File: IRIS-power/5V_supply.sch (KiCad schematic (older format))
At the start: 8 parts

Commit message: Finalized power board V2 schematic, preparing to layout
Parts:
- C501, C502: renamed from C?; footprint (none) -> Capacitor_SMD:C_0603_1608Metric
- C503, C504: renamed from C?; footprint (none) -> Capacitor_SMD:C_1210_3225Metric
- NT501: renamed from NT?; footprint (none) -> NetTie:NetTie-2_SMD_Pad0.5mm
- R501, R502: renamed from R?; footprint (none) -> Resistor_SMD:R_0603_1608Metric
- U501: renamed from U?; footprint (none) -> star-common-lib:TPSM53604
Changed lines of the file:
@@
 $Descr A4 11693 8268
 encoding utf-8
-Sheet 4 9
+Sheet 5 8
 Title ""
 Date ""
@@
 P 5700 3950
 AR Path="/5F427B86" Ref="U?"  Part="1"
-AR Path="/5F41B5C3/5F427B86" Ref="U?"  Part="1"
-F 0 "U?" H 5700 4400 50  0000 C CNN
+AR Path="/5F41B5C3/5F427B86" Ref="U501"  Part="1"
+F 0 "U501" H 5700 4400 50  0000 C CNN
 F 1 "TPSM53604" H 5700 4300 50  0000 C CNN
-F 2 "" H 5700 3950 50  0001 C CNN
+F 2 "star-common-lib:TPSM53604" H 5700 3950 50  0001 C CNN
 F 3 "" H 5700 3950 50  0001 C CNN
 	1    5700 3950
@@
 P 5650 4400
 AR Path="/5F427B91" Ref="NT?"  Part="1"
-AR Path="/5F41B5C3/5F427B91" Ref="NT?"  Part="1"
-F 0 "NT?" H 5650 4489 50  0000 C CNN
+AR Path="/5F41B5C3/5F427B91" Ref="NT501"  Part="1"
+F 0 "NT501" H 5650 4489 50  0000 C CNN
 F 1 "Net-Tie_2" H 5650 4490 50  0001 C CNN
-F 2 "" H 5650 4400 50  0001 C CNN
+F 2 "NetTie:NetTie-2_SMD_Pad0.5mm" H 5650 4400 50  0001 C CNN
 F 3 "~" H 5650 4400 50  0001 C CNN
 	1    5650 4400
@@
 P 5500 4400
 AR Path="/5F427B99" Ref="#PWR?"  Part="1"
-AR Path="/5F41B5C3/5F427B99" Ref="#PWR?"  Part="1"
-F 0 "#PWR?" H 5500 4150 50  0001 C CNN
+AR Path="/5F41B5C3/5F427B99" Ref="#PWR0502"  Part="1"
+F 0 "#PWR0502" H 5500 4150 50  0001 C CNN
 F 1 "GND" H 5505 4227 50  0000 C CNN
 F 2 "" H 5500 4400 50  0001 C CNN
@@
 P 4800 3900
 AR Path="/5F427BA2" Ref="C?"  Part="1"
-AR Path="/5F41B5C3/5F427BA2" Ref="C?"  Part="1"
-F 0 "C?" H 4915 3946 50  0000 L CNN
+AR Path="/5F41B5C3/5F427BA2" Ref="C502"  Part="1"
+F 0 "C502" H 4915 3946 50  0000 L CNN
 F 1 "10uF" H 4915 3855 50  0000 L CNN
-F 2 "" H 4838 3750 50  0001 C CNN
+F 2 "Capacitor_SMD:C_0603_1608Metric" H 4838 3750 50  0001 C CNN
 F 3 "~" H 4800 3900 50  0001 C CNN
 	1    4800 3900
@@
 P 4400 3900
 AR Path="/5F427BA8" Ref="C?"  Part="1"
-AR Path="/5F41B5C3/5F427BA8" Ref="C?"  Part="1"
-F 0 "C?" H 4515 3946 50  0000 L CNN
+AR Path="/5F41B5C3/5F427BA8" Ref="C501"  Part="1"
+F 0 "C501" H 4515 3946 50  0000 L CNN
 F 1 "10uF" H 4515 3855 50  0000 L CNN
-F 2 "" H 4438 3750 50  0001 C CNN
+F 2 "Capacitor_SMD:C_0603_1608Metric" H 4438 3750 50  0001 C CNN
 F 3 "~" H 4400 3900 50  0001 C CNN
 	1    4400 3900
@@
 P 6550 3900
 AR Path="/5F427BB2" Ref="R?"  Part="1"
-AR Path="/5F41B5C3/5F427BB2" Ref="R?"  Part="1"
-F 0 "R?" H 6620 3946 50  0000 L CNN
+AR Path="/5F41B5C3/5F427BB2" Ref="R501"  Part="1"
+F 0 "R501" H 6620 3946 50  0000 L CNN
 F 1 "10k" H 6620 3855 50  0000 L CNN
-F 2 "" V 6480 3900 50  0001 C CNN
+F 2 "Resistor_SMD:R_0603_1608Metric" V 6480 3900 50  0001 C CNN
 F 3 "~" H 6550 3900 50  0001 C CNN
 	1    6550 3900
@@
 P 6550 4200
 AR Path="/5F427BB8" Ref="R?"  Part="1"
-AR Path="/5F41B5C3/5F427BB8" Ref="R?"  Part="1"
-F 0 "R?" H 6620 4246 50  0000 L CNN
+AR Path="/5F41B5C3/5F427BB8" Ref="R502"  Part="1"
+F 0 "R502" H 6620 4246 50  0000 L CNN
 F 1 "2.49k" H 6620 4155 50  0000 L CNN
-F 2 "" V 6480 4200 50  0001 C CNN
+F 2 "Resistor_SMD:R_0603_1608Metric" V 6480 4200 50  0001 C CNN
 F 3 "~" H 6550 4200 50  0001 C CNN
 	1    6550 4200
@@
 P 6900 3900
 AR Path="/5F427BC1" Ref="C?"  Part="1"
-AR Path="/5F41B5C3/5F427BC1" Ref="C?"  Part="1"
-F 0 "C?" H 7015 3946 50  0000 L CNN
+AR Path="/5F41B5C3/5F427BC1" Ref="C503"  Part="1"
+F 0 "C503" H 7015 3946 50  0000 L CNN
 F 1 "47uF" H 7015 3855 50  0000 L CNN
-F 2 "" H 6938 3750 50  0001 C CNN
+F 2 "Capacitor_SMD:C_1210_3225Metric" H 6938 3750 50  0001 C CNN
 F 3 "~" H 6900 3900 50  0001 C CNN
 	1    6900 3900
@@
 P 7300 3900
 AR Path="/5F427BC7" Ref="C?"  Part="1"
-AR Path="/5F41B5C3/5F427BC7" Ref="C?"  Part="1"
-F 0 "C?" H 7415 3946 50  0000 L CNN
+AR Path="/5F41B5C3/5F427BC7" Ref="C504"  Part="1"
+F 0 "C504" H 7415 3946 50  0000 L CNN
 F 1 "47uF" H 7415 3855 50  0000 L CNN
-F 2 "" H 7338 3750 50  0001 C CNN
+F 2 "Capacitor_SMD:C_1210_3225Metric" H 7338 3750 50  0001 C CNN
 F 3 "~" H 7300 3900 50  0001 C CNN
 	1    7300 3900
@@
 P 4600 4050
 AR Path="/5F427BCD" Ref="#PWR?"  Part="1"
-AR Path="/5F41B5C3/5F427BCD" Ref="#PWR?"  Part="1"
-F 0 "#PWR?" H 4600 3800 50  0001 C CNN
+AR Path="/5F41B5C3/5F427BCD" Ref="#PWR0501"  Part="1"
+F 0 "#PWR0501" H 4600 3800 50  0001 C CNN
 F 1 "GND" H 4605 3877 50  0000 C CNN
 F 2 "" H 4600 4050 50  0001 C CNN
@@
 P 7100 4050
 AR Path="/5F427BD6" Ref="#PWR?"  Part="1"
-AR Path="/5F41B5C3/5F427BD6" Ref="#PWR?"  Part="1"
-F 0 "#PWR?" H 7100 3800 50  0001 C CNN
+AR Path="/5F41B5C3/5F427BD6" Ref="#PWR0503"  Part="1"
+F 0 "#PWR0503" H 7100 3800 50  0001 C CNN
 F 1 "GND" H 7105 3877 50  0000 C CNN
 F 2 "" H 7100 4050 50  0001 C CNN

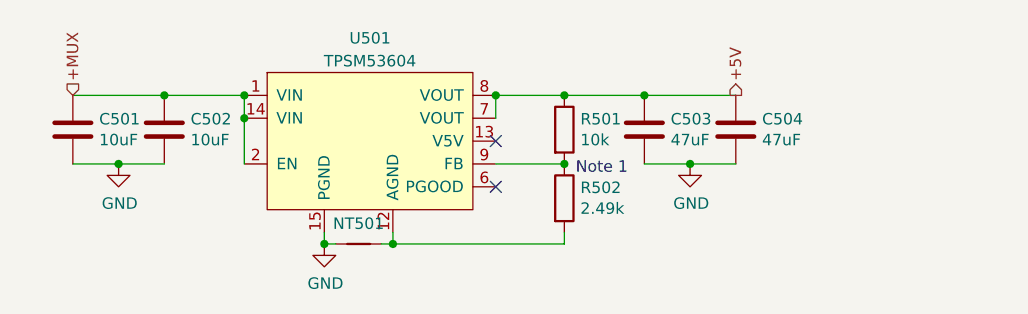
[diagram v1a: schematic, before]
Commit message: Updated layout
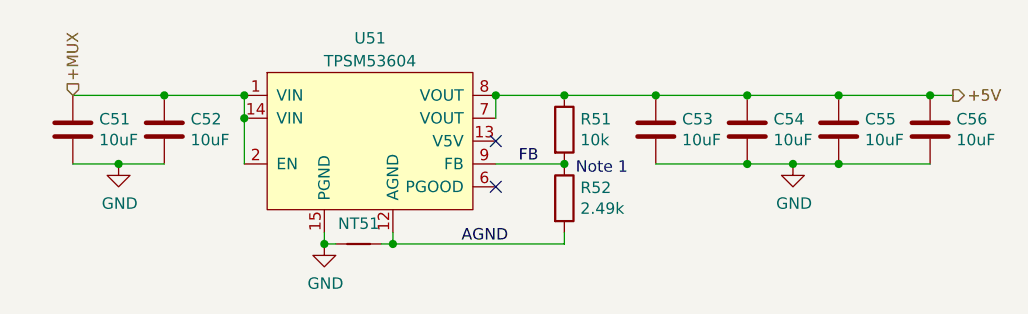
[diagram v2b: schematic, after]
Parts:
- removed C503, C504: 47uF, Capacitor_SMD:C_1210_3225Metric, symbol Device:C
- added C53, C54, C55, C56: 10uF, Capacitor_SMD:C_0603_1608Metric, symbol Device:C
- renumbered C501 to C51, C502 to C52, NT501 to NT51, R501 to R51, R502 to R52, U501 to U51
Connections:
- net +5V: now also C53.1, C54.1, C55.1, C56.1
- net GND: now also C53.2, C54.2, C55.2, C56.2
- net AGND: now reaches NT51.2, R52.2, U51.12 (AGND)
- net FB: now reaches R51.2, R52.1, U51.9 (FB)
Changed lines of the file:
@@
 P 5700 3950
 AR Path="/5F427B86" Ref="U?"  Part="1"
-AR Path="/5F41B5C3/5F427B86" Ref="U501"  Part="1"
-F 0 "U501" H 5700 4400 50  0000 C CNN
+AR Path="/5F41B5C3/5F427B86" Ref="U51"  Part="1"
+F 0 "U51" H 5700 4400 50  0000 C CNN
 F 1 "TPSM53604" H 5700 4300 50  0000 C CNN
 F 2 "star-common-lib:TPSM53604" H 5700 3950 50  0001 C CNN
@@
 P 5650 4400
 AR Path="/5F427B91" Ref="NT?"  Part="1"
-AR Path="/5F41B5C3/5F427B91" Ref="NT501"  Part="1"
-F 0 "NT501" H 5650 4489 50  0000 C CNN
+AR Path="/5F41B5C3/5F427B91" Ref="NT51"  Part="1"
+F 0 "NT51" H 5650 4489 50  0000 C CNN
 F 1 "Net-Tie_2" H 5650 4490 50  0001 C CNN
 F 2 "NetTie:NetTie-2_SMD_Pad0.5mm" H 5650 4400 50  0001 C CNN
@@
 P 5500 4400
 AR Path="/5F427B99" Ref="#PWR?"  Part="1"
-AR Path="/5F41B5C3/5F427B99" Ref="#PWR0502"  Part="1"
-F 0 "#PWR0502" H 5500 4150 50  0001 C CNN
+AR Path="/5F41B5C3/5F427B99" Ref="#PWR052"  Part="1"
+F 0 "#PWR052" H 5500 4150 50  0001 C CNN
 F 1 "GND" H 5505 4227 50  0000 C CNN
 F 2 "" H 5500 4400 50  0001 C CNN
@@
 P 4800 3900
 AR Path="/5F427BA2" Ref="C?"  Part="1"
-AR Path="/5F41B5C3/5F427BA2" Ref="C502"  Part="1"
-F 0 "C502" H 4915 3946 50  0000 L CNN
+AR Path="/5F41B5C3/5F427BA2" Ref="C52"  Part="1"
+F 0 "C52" H 4915 3946 50  0000 L CNN
 F 1 "10uF" H 4915 3855 50  0000 L CNN
 F 2 "Capacitor_SMD:C_0603_1608Metric" H 4838 3750 50  0001 C CNN
@@
 P 4400 3900
 AR Path="/5F427BA8" Ref="C?"  Part="1"
-AR Path="/5F41B5C3/5F427BA8" Ref="C501"  Part="1"
-F 0 "C501" H 4515 3946 50  0000 L CNN
+AR Path="/5F41B5C3/5F427BA8" Ref="C51"  Part="1"
+F 0 "C51" H 4515 3946 50  0000 L CNN
 F 1 "10uF" H 4515 3855 50  0000 L CNN
 F 2 "Capacitor_SMD:C_0603_1608Metric" H 4438 3750 50  0001 C CNN
@@
 P 6550 3900
 AR Path="/5F427BB2" Ref="R?"  Part="1"
-AR Path="/5F41B5C3/5F427BB2" Ref="R501"  Part="1"
-F 0 "R501" H 6620 3946 50  0000 L CNN
+AR Path="/5F41B5C3/5F427BB2" Ref="R51"  Part="1"
+F 0 "R51" H 6620 3946 50  0000 L CNN
 F 1 "10k" H 6620 3855 50  0000 L CNN
 F 2 "Resistor_SMD:R_0603_1608Metric" V 6480 3900 50  0001 C CNN
@@
 P 6550 4200
 AR Path="/5F427BB8" Ref="R?"  Part="1"
-AR Path="/5F41B5C3/5F427BB8" Ref="R502"  Part="1"
-F 0 "R502" H 6620 4246 50  0000 L CNN
+AR Path="/5F41B5C3/5F427BB8" Ref="R52"  Part="1"
+F 0 "R52" H 6620 4246 50  0000 L CNN
 F 1 "2.49k" H 6620 4155 50  0000 L CNN
 F 2 "Resistor_SMD:R_0603_1608Metric" V 6480 4200 50  0001 C CNN
@@
 Connection ~ 6550 4050
 $Comp
-L Device:C C?
-U 1 1 5F427BC1
-P 6900 3900
-AR Path="/5F427BC1" Ref="C?"  Part="1"
-AR Path="/5F41B5C3/5F427BC1" Ref="C503"  Part="1"
-F 0 "C503" H 7015 3946 50  0000 L CNN
-F 1 "47uF" H 7015 3855 50  0000 L CNN
-F 2 "Capacitor_SMD:C_1210_3225Metric" H 6938 3750 50  0001 C CNN
-F 3 "~" H 6900 3900 50  0001 C CNN
-	1    6900 3900
-	1    0    0    -1
-$EndComp
-$Comp
-L Device:C C?
-U 1 1 5F427BC7
-P 7300 3900
-AR Path="/5F427BC7" Ref="C?"  Part="1"
-AR Path="/5F41B5C3/5F427BC7" Ref="C504"  Part="1"
-F 0 "C504" H 7415 3946 50  0000 L CNN
-F 1 "47uF" H 7415 3855 50  0000 L CNN
-F 2 "Capacitor_SMD:C_1210_3225Metric" H 7338 3750 50  0001 C CNN
-F 3 "~" H 7300 3900 50  0001 C CNN
-	1    7300 3900
-	1    0    0    -1
-$EndComp
-$Comp
 L power:GND #PWR?
 U 1 1 5F427BCD
 P 4600 4050
 AR Path="/5F427BCD" Ref="#PWR?"  Part="1"
-AR Path="/5F41B5C3/5F427BCD" Ref="#PWR0501"  Part="1"
-F 0 "#PWR0501" H 4600 3800 50  0001 C CNN
+AR Path="/5F41B5C3/5F427BCD" Ref="#PWR051"  Part="1"
+F 0 "#PWR051" H 4600 3800 50  0001 C CNN
 F 1 "GND" H 4605 3877 50  0000 C CNN
 F 2 "" H 4600 4050 50  0001 C CNN
@@
 L power:GND #PWR?
 U 1 1 5F427BD6
-P 7100 4050
+P 7550 4050
 AR Path="/5F427BD6" Ref="#PWR?"  Part="1"
-AR Path="/5F41B5C3/5F427BD6" Ref="#PWR0503"  Part="1"
-F 0 "#PWR0503" H 7100 3800 50  0001 C CNN
-F 1 "GND" H 7105 3877 50  0000 C CNN
-F 2 "" H 7100 4050 50  0001 C CNN
-F 3 "" H 7100 4050 50  0001 C CNN
-	1    7100 4050
-	1    0    0    -1
-$EndComp
-Wire Wire Line
-	6900 4050 7100 4050
-Connection ~ 7100 4050
-Wire Wire Line
-	7100 4050 7300 4050
+AR Path="/5F41B5C3/5F427BD6" Ref="#PWR053"  Part="1"
+F 0 "#PWR053" H 7550 3800 50  0001 C CNN
+F 1 "GND" H 7555 3877 50  0000 C CNN
+F 2 "" H 7550 4050 50  0001 C CNN
+F 3 "" H 7550 4050 50  0001 C CNN
+	1    7550 4050
+	1    0    0    -1
+$EndComp
+Wire Wire Line
+	7350 4050 7550 4050
+Connection ~ 7550 4050
+Wire Wire Line
+	7550 4050 7750 4050
 Wire Wire Line
 	5800 4400 6550 4400
@@
 	6550 4400 6550 4350
 Connection ~ 5800 4400
-Wire Wire Line
-	6550 3750 6900 3750
 Connection ~ 6550 3750
-Connection ~ 6900 3750
-Wire Wire Line
-	6900 3750 7300 3750
 NoConn ~ 6250 4150
 Wire Wire Line
@@
 Text HLabel 4400 3750 1    50   Input ~ 0
 +MUX
-Text HLabel 7300 3750 1    50   Output ~ 0
+Text HLabel 8250 3750 2    50   Output ~ 0
 +5V
+Text Label 6350 4050 0    50   ~ 0
+FB
+Text Label 6100 4400 0    50   ~ 0
+AGND
+$Comp
+L Device:C C53
+U 1 1 5F353A91
+P 6950 3900
+F 0 "C53" H 7065 3946 50  0000 L CNN
+F 1 "10uF" H 7065 3855 50  0000 L CNN
+F 2 "Capacitor_SMD:C_0603_1608Metric" H 6988 3750 50  0001 C CNN
+F 3 "~" H 6950 3900 50  0001 C CNN
+	1    6950 3900
+	1    0    0    -1
+$EndComp
+$Comp
+L Device:C C54
+U 1 1 5F353D55
+P 7350 3900
+F 0 "C54" H 7465 3946 50  0000 L CNN
+F 1 "10uF" H 7465 3855 50  0000 L CNN
+F 2 "Capacitor_SMD:C_0603_1608Metric" H 7388 3750 50  0001 C CNN
+F 3 "~" H 7350 3900 50  0001 C CNN
+	1    7350 3900
+	1    0    0    -1
+$EndComp
+$Comp
+L Device:C C55
+U 1 1 5F3540F0
+P 7750 3900
+F 0 "C55" H 7865 3946 50  0000 L CNN
+F 1 "10uF" H 7865 3855 50  0000 L CNN
+F 2 "Capacitor_SMD:C_0603_1608Metric" H 7788 3750 50  0001 C CNN
+F 3 "~" H 7750 3900 50  0001 C CNN
+	1    7750 3900
+	1    0    0    -1
+$EndComp
+$Comp
+L Device:C C56
+U 1 1 5F354331
+P 8150 3900
+F 0 "C56" H 8265 3946 50  0000 L CNN
+F 1 "10uF" H 8265 3855 50  0000 L CNN
+F 2 "Capacitor_SMD:C_0603_1608Metric" H 8188 3750 50  0001 C CNN
+F 3 "~" H 8150 3900 50  0001 C CNN
+	1    8150 3900
+	1    0    0    -1
+$EndComp
+Wire Wire Line
+	6550 3750 6950 3750
+Wire Wire Line
+	7350 4050 6950 4050
+Connection ~ 7350 4050
+Wire Wire Line
+	7750 4050 8150 4050
+Connection ~ 7750 4050
+Connection ~ 6950 3750
+Wire Wire Line
+	6950 3750 7350 3750
+Connection ~ 7350 3750
+Wire Wire Line
+	7350 3750 7750 3750
+Connection ~ 7750 3750
+Wire Wire Line
+	7750 3750 8150 3750
+Connection ~ 8150 3750
+Wire Wire Line
+	8150 3750 8250 3750
 $EndSCHEMATC

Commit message: Added some 3D models
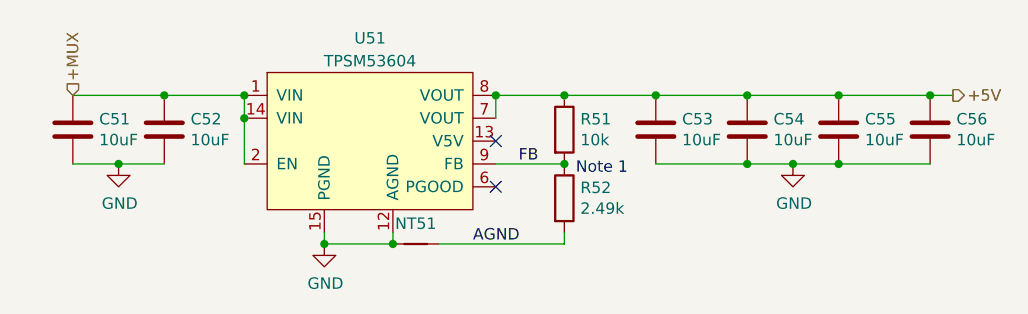
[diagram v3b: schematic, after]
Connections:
- net AGND: no longer U51.12 (AGND)
- net GND: now also U51.12 (AGND)
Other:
- moved on the sheet: NT51
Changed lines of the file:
@@
 L Device:Net-Tie_2 NT?
 U 1 1 5F427B91
-P 5650 4400
+P 5900 4400
 AR Path="/5F427B91" Ref="NT?"  Part="1"
 AR Path="/5F41B5C3/5F427B91" Ref="NT51"  Part="1"
-F 0 "NT51" H 5650 4489 50  0000 C CNN
-F 1 "Net-Tie_2" H 5650 4490 50  0001 C CNN
-F 2 "NetTie:NetTie-2_SMD_Pad0.5mm" H 5650 4400 50  0001 C CNN
-F 3 "~" H 5650 4400 50  0001 C CNN
-	1    5650 4400
-	1    0    0    -1
-$EndComp
-Wire Wire Line
-	5750 4400 5800 4400
+F 0 "NT51" H 5900 4489 50  0000 C CNN
+F 1 "Net-Tie_2" H 5900 4490 50  0001 C CNN
+F 2 "NetTie:NetTie-2_SMD_Pad0.5mm" H 5900 4400 50  0001 C CNN
+F 3 "~" H 5900 4400 50  0001 C CNN
+	1    5900 4400
+	1    0    0    -1
+$EndComp
 Wire Wire Line
 	5800 4400 5800 4350
@@
 Wire Wire Line
 	5500 4350 5500 4400
-Wire Wire Line
-	5500 4400 5550 4400
 Connection ~ 5500 4400
 $Comp
@@
 	7550 4050 7750 4050
 Wire Wire Line
-	5800 4400 6550 4400
-Wire Wire Line
 	6550 4400 6550 4350
-Connection ~ 5800 4400
 Connection ~ 6550 3750
 NoConn ~ 6250 4150
@@
 Text Label 6350 4050 0    50   ~ 0
 FB
-Text Label 6100 4400 0    50   ~ 0
+Text Label 6150 4400 0    50   ~ 0
 AGND
 $Comp
@@
 Wire Wire Line
 	8150 3750 8250 3750
+Wire Wire Line
+	6000 4400 6550 4400
+Wire Wire Line
+	5500 4400 5800 4400
+Connection ~ 5800 4400
 $EndSCHEMATC

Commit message: Improved fuel gauge layout
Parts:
- C51, C52, C53, C54, C55, C56: Digikey PN (none) -> 1276-1192-1-ND
- R51: Digikey PN (none) -> RNCP0603FTD10K0CT-ND
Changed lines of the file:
@@
 F 2 "Capacitor_SMD:C_0603_1608Metric" H 4838 3750 50  0001 C CNN
 F 3 "~" H 4800 3900 50  0001 C CNN
+F 4 "1276-1192-1-ND" H 4800 3900 50  0001 C CNN "Digikey PN"
 	1    4800 3900
 	1    0    0    -1
@@
 F 2 "Capacitor_SMD:C_0603_1608Metric" H 4438 3750 50  0001 C CNN
 F 3 "~" H 4400 3900 50  0001 C CNN
+F 4 "1276-1192-1-ND" H 4400 3900 50  0001 C CNN "Digikey PN"
 	1    4400 3900
 	1    0    0    -1
@@
 F 2 "Resistor_SMD:R_0603_1608Metric" V 6480 3900 50  0001 C CNN
 F 3 "~" H 6550 3900 50  0001 C CNN
+F 4 "RNCP0603FTD10K0CT-ND" H 6550 3900 50  0001 C CNN "Digikey PN"
 	1    6550 3900
 	1    0    0    -1
@@
 F 2 "Capacitor_SMD:C_0603_1608Metric" H 6988 3750 50  0001 C CNN
 F 3 "~" H 6950 3900 50  0001 C CNN
+F 4 "1276-1192-1-ND" H 6950 3900 50  0001 C CNN "Digikey PN"
 	1    6950 3900
 	1    0    0    -1
@@
 F 2 "Capacitor_SMD:C_0603_1608Metric" H 7388 3750 50  0001 C CNN
 F 3 "~" H 7350 3900 50  0001 C CNN
+F 4 "1276-1192-1-ND" H 7350 3900 50  0001 C CNN "Digikey PN"
 	1    7350 3900
 	1    0    0    -1
@@
 F 2 "Capacitor_SMD:C_0603_1608Metric" H 7788 3750 50  0001 C CNN
 F 3 "~" H 7750 3900 50  0001 C CNN
+F 4 "1276-1192-1-ND" H 7750 3900 50  0001 C CNN "Digikey PN"
 	1    7750 3900
 	1    0    0    -1
@@
 F 2 "Capacitor_SMD:C_0603_1608Metric" H 8188 3750 50  0001 C CNN
 F 3 "~" H 8150 3900 50  0001 C CNN
+F 4 "1276-1192-1-ND" H 8150 3900 50  0001 C CNN "Digikey PN"
 	1    8150 3900
 	1    0    0    -1

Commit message: Adjusted silkscreen
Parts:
- R52: Digikey PN (none) -> RNCP0603FTD2K49CT-ND
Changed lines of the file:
@@
 F 2 "Resistor_SMD:R_0603_1608Metric" V 6480 4200 50  0001 C CNN
 F 3 "~" H 6550 4200 50  0001 C CNN
+F 4 "RNCP0603FTD2K49CT-ND" H 6550 4200 50  0001 C CNN "Digikey PN"
 	1    6550 4200
 	1    0    0    -1

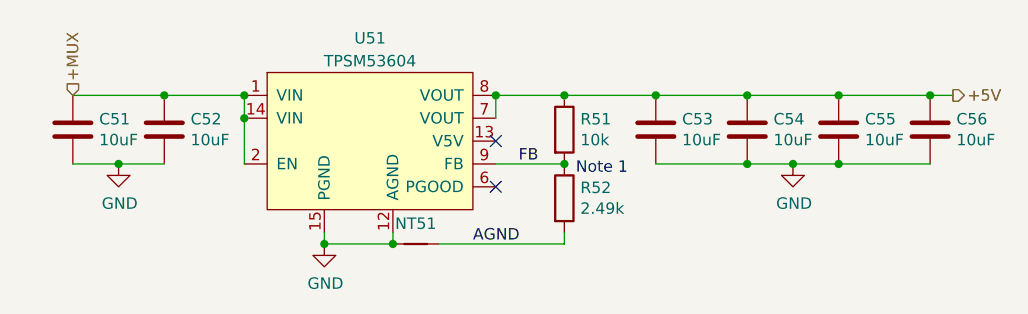
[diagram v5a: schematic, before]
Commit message: USB C power prototype
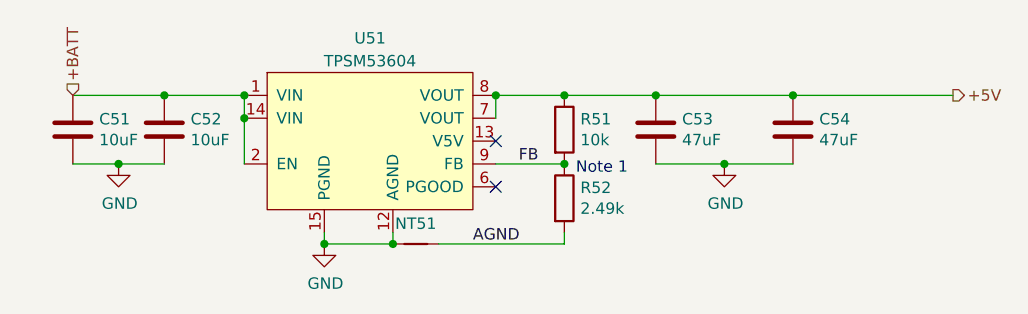
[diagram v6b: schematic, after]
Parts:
- removed C55, C56: 10uF, Capacitor_SMD:C_0603_1608Metric, symbol Device:C
- C53, C54: value 10uF -> 47uF; footprint Capacitor_SMD:C_0603_1608Metric -> Capacitor_SMD:C_1206_3216Metric; Digikey PN 1276-1192-1-ND -> (none)
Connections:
- net +MUX renamed +BATT
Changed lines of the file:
@@
 $Descr A4 11693 8268
 encoding utf-8
-Sheet 5 8
+Sheet 5 9
 Title ""
 Date ""
@@
 L power:GND #PWR?
 U 1 1 5F427BD6
-P 7550 4050
+P 7250 4050
 AR Path="/5F427BD6" Ref="#PWR?"  Part="1"
 AR Path="/5F41B5C3/5F427BD6" Ref="#PWR053"  Part="1"
-F 0 "#PWR053" H 7550 3800 50  0001 C CNN
-F 1 "GND" H 7555 3877 50  0000 C CNN
-F 2 "" H 7550 4050 50  0001 C CNN
-F 3 "" H 7550 4050 50  0001 C CNN
-	1    7550 4050
-	1    0    0    -1
-$EndComp
-Wire Wire Line
-	7350 4050 7550 4050
-Connection ~ 7550 4050
-Wire Wire Line
-	7550 4050 7750 4050
+F 0 "#PWR053" H 7250 3800 50  0001 C CNN
+F 1 "GND" H 7255 3877 50  0000 C CNN
+F 2 "" H 7250 4050 50  0001 C CNN
+F 3 "" H 7250 4050 50  0001 C CNN
+	1    7250 4050
+	1    0    0    -1
+$EndComp
 Wire Wire Line
 	6550 4400 6550 4350
@@
 Note 1
 Text HLabel 4400 3750 1    50   Input ~ 0
-+MUX
++BATT
 Text HLabel 8250 3750 2    50   Output ~ 0
 +5V
@@
 Text Label 6150 4400 0    50   ~ 0
 AGND
+Wire Wire Line
+	6000 4400 6550 4400
+Wire Wire Line
+	5500 4400 5800 4400
+Connection ~ 5800 4400
+Wire Wire Line
+	6950 4050 7250 4050
+Wire Wire Line
+	6550 3750 6950 3750
 $Comp
 L Device:C C53
-U 1 1 5F353A91
+U 1 1 5FBDF297
 P 6950 3900
 F 0 "C53" H 7065 3946 50  0000 L CNN
-F 1 "10uF" H 7065 3855 50  0000 L CNN
-F 2 "Capacitor_SMD:C_0603_1608Metric" H 6988 3750 50  0001 C CNN
+F 1 "47uF" H 7065 3855 50  0000 L CNN
+F 2 "Capacitor_SMD:C_1206_3216Metric" H 6988 3750 50  0001 C CNN
 F 3 "~" H 6950 3900 50  0001 C CNN
-F 4 "1276-1192-1-ND" H 6950 3900 50  0001 C CNN "Digikey PN"
 	1    6950 3900
 	1    0    0    -1
 $EndComp
+Connection ~ 6950 3750
+Wire Wire Line
+	6950 3750 7550 3750
 $Comp
 L Device:C C54
-U 1 1 5F353D55
-P 7350 3900
-F 0 "C54" H 7465 3946 50  0000 L CNN
-F 1 "10uF" H 7465 3855 50  0000 L CNN
-F 2 "Capacitor_SMD:C_0603_1608Metric" H 7388 3750 50  0001 C CNN
-F 3 "~" H 7350 3900 50  0001 C CNN
-F 4 "1276-1192-1-ND" H 7350 3900 50  0001 C CNN "Digikey PN"
-	1    7350 3900
-	1    0    0    -1
-$EndComp
-$Comp
-L Device:C C55
-U 1 1 5F3540F0
-P 7750 3900
-F 0 "C55" H 7865 3946 50  0000 L CNN
-F 1 "10uF" H 7865 3855 50  0000 L CNN
-F 2 "Capacitor_SMD:C_0603_1608Metric" H 7788 3750 50  0001 C CNN
-F 3 "~" H 7750 3900 50  0001 C CNN
-F 4 "1276-1192-1-ND" H 7750 3900 50  0001 C CNN "Digikey PN"
-	1    7750 3900
-	1    0    0    -1
-$EndComp
-$Comp
-L Device:C C56
-U 1 1 5F354331
-P 8150 3900
-F 0 "C56" H 8265 3946 50  0000 L CNN
-F 1 "10uF" H 8265 3855 50  0000 L CNN
-F 2 "Capacitor_SMD:C_0603_1608Metric" H 8188 3750 50  0001 C CNN
-F 3 "~" H 8150 3900 50  0001 C CNN
-F 4 "1276-1192-1-ND" H 8150 3900 50  0001 C CNN "Digikey PN"
-	1    8150 3900
-	1    0    0    -1
-$EndComp
-Wire Wire Line
-	6550 3750 6950 3750
-Wire Wire Line
-	7350 4050 6950 4050
-Connection ~ 7350 4050
-Wire Wire Line
-	7750 4050 8150 4050
-Connection ~ 7750 4050
-Connection ~ 6950 3750
-Wire Wire Line
-	6950 3750 7350 3750
-Connection ~ 7350 3750
-Wire Wire Line
-	7350 3750 7750 3750
-Connection ~ 7750 3750
-Wire Wire Line
-	7750 3750 8150 3750
-Connection ~ 8150 3750
-Wire Wire Line
-	8150 3750 8250 3750
-Wire Wire Line
-	6000 4400 6550 4400
-Wire Wire Line
-	5500 4400 5800 4400
-Connection ~ 5800 4400
+U 1 1 5FBDF68D
+P 7550 3900
+F 0 "C54" H 7665 3946 50  0000 L CNN
+F 1 "47uF" H 7665 3855 50  0000 L CNN
+F 2 "Capacitor_SMD:C_1206_3216Metric" H 7588 3750 50  0001 C CNN
+F 3 "~" H 7550 3900 50  0001 C CNN
+	1    7550 3900
+	1    0    0    -1
+$EndComp
+Connection ~ 7550 3750
+Wire Wire Line
+	7550 3750 8250 3750
+Connection ~ 7250 4050
+Wire Wire Line
+	7250 4050 7550 4050
 $EndSCHEMATC
